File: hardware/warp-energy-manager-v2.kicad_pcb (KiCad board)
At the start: 4 copper layers, 68 x 87 mm, 118 parts, among them J101 Boot, J102 DM3CS, P101 CON-SENSOR2, P102 SG-Ready, P103 L+N, P104 OUT, P105 INPUT, P110 MODBUS, P111 Debug, Q101 2N7002P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

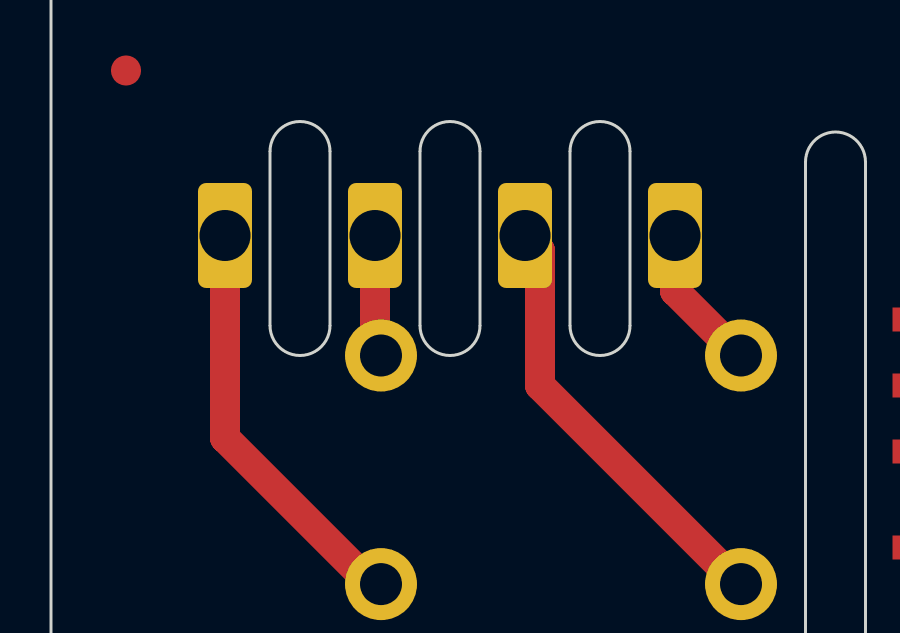
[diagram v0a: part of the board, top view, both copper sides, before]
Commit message: add 3d models
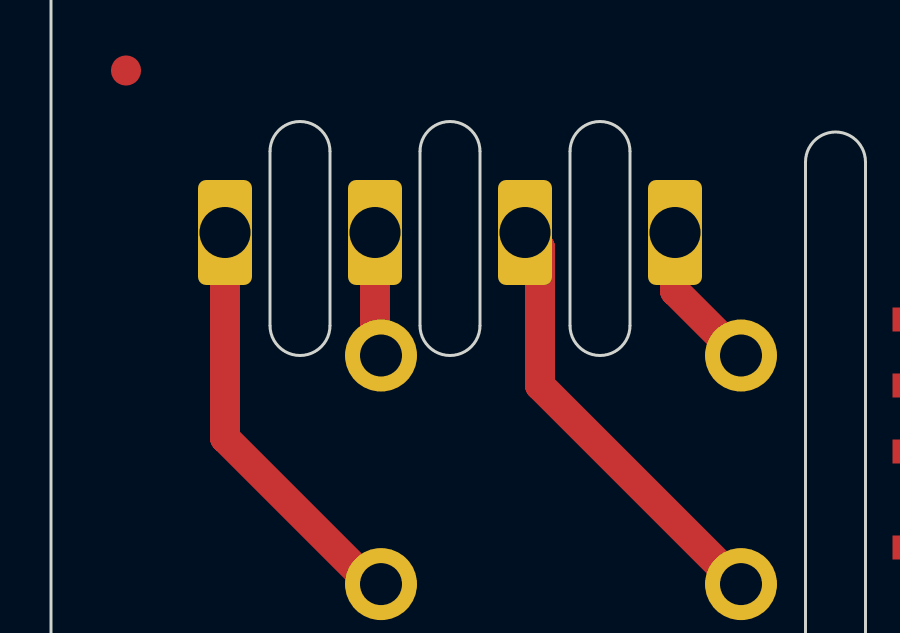
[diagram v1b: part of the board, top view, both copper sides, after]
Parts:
- R104, R105, R115, R116: value 1k -> 2k2
- R112, R117, R120, R121: value 1k -> 680
- moved P104 0.10 mm to (105.7, 61.0)
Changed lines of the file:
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@@
 			(sketchpadsonfab no)
 			(subtractmaskfromsilk yes)
-			(outputformat 3)
+			(outputformat 1)
 			(mirror no)
 			(drillshape 0)
@@
 			(pintype "passive")
 		)
+		(model "${KICAD6_3DMODEL_DIR}/Connectors/OQ_2P_5mm_230V.step"
+			(offset
+				(xyz 0 0 0)
+			)
+			(scale
+				(xyz 1 1 1)
+			)
+			(rotate
+				(xyz 0 0 0)
+			)
+		)
 	)
 	(footprint "kicad-libraries:C0402F"
@@
 		)
 		(property "Value" "100uF"
-			(at 0 1.95072 90)
+			(at -0.00112 0.55 90)
 			(layer "F.Fab")
 			(effects
@@
 		(tags "CMS SOT")
 		(property "Reference" "Q105"
-			(at -0.925 0 180)
+			(at -1.05 0 180)
 			(layer "F.Fab")
 			(effects
@@
 		)
 		(property "Value" "SSM3J355R,LF"
-			(at 0.775 0 180)
+			(at 0.45 0 180)
 			(layer "F.Fab")
 			(effects
@@
 			(pintype "input")
 		)
+		(model "${KICAD6_3DMODEL_DIR}/unsorted/G5Q_1A.step"
+			(offset
+				(xyz 0 0 0)
+			)
+			(scale
+				(xyz 1 1 1)
+			)
+			(rotate
+				(xyz 0 0 0)
+			)
+		)
 	)
 	(footprint "kicad-libraries:MiniMelf"
@@
 			)
 		)
-		(property "Value" "1k"
+		(property "Value" "680"
 			(at 0 -0.4 -90)
 			(layer "F.Fab")
@@
 	(footprint "kicad-libraries:OQ_4P_5mm_230V"
 		(layer "F.Cu")
-		(at 105.65 61.05 180)
+		(at 105.65 60.95 180)
 		(property "Reference" "P104"
 			(at 0 3.5 180)
@@
 			(pintype "passive")
 		)
+		(model "${KICAD6_3DMODEL_DIR}/Connectors/OQ_4P_5mm_230V.step"
+			(offset
+				(xyz 0 0 0)
+			)
+			(scale
+				(xyz 1 1 1)
+			)
+			(rotate
+				(xyz 0 0 0)
+			)
+		)
 	)
 	(footprint "kicad-libraries:SOT23GDS"
@@
 			(pintype "passive")
 		)
+		(model "${KICAD6_3DMODEL_DIR}/unsorted/AGQ2X0.step"
+			(offset
+				(xyz 0 0 0)
+			)
+			(scale
+				(xyz 1 1 1)
+			)
+			(rotate
+				(xyz 0 0 0)
+			)
+		)
 	)
 	(footprint "kicad-libraries:R0603F"
@@
 			)
 		)
-		(property "Value" "1k"
+		(property "Value" "680"
 			(at 0 -0.4 -90)
 			(layer "F.Fab")
@@
 		)
 		(property "Value" "SMAJ12CA"
-			(at -0.71 0.12 0)
+			(at -0.9 0 0)
 			(layer "F.Fab")
 			(effects
@@
 			)
 		)
-		(property "Value" "1k"
+		(property "Value" "680"
 			(at 0 -0.4 -90)
 			(layer "F.Fab")
@@
 			)
 		)
-		(property "Value" "1k"
+		(property "Value" "2k2"
 			(at 0 -0.4 -90)
 			(layer "F.Fab")
@@
 			(pintype "passive")
 		)
+		(model "${KICAD6_3DMODEL_DIR}/unsorted/AGQ2X0.step"
+			(offset
+				(xyz 0 0 0)
+			)
+			(scale
+				(xyz 1 1 1)
+			)
+			(rotate
+				(xyz 0 0 0)
+			)
+		)
 	)
 	(footprint "kicad-libraries:SOT23GDS"
@@
 		(tags "CMS SOT")
 		(property "Reference" "Q101"
-			(at 1 -0.5 0)
+			(at -0.6 0 0)
 			(layer "F.Fab")
 			(effects
@@
 		)
 		(property "Value" "2N7002P"
-			(at 1 0 0)
+			(at 0.8 0 0)
 			(layer "F.Fab")
 			(effects
@@
 			)
 		)
-		(property "Value" "1k"
+		(property "Value" "2k2"
 			(at 0 -0.4 -90)
 			(layer "F.Fab")
@@
 		)
 		(property "Value" "SMAJ12CA"
-			(at -0.71 0.12 180)
+			(at -0.9 0.12 180)
 			(layer "F.Fab")
 			(effects
@@
 			)
 		)
-		(property "Value" "1k"
+		(property "Value" "2k2"
 			(at 0 -0.4 -90)
 			(layer "F.Fab")
@@
 			)
 		)
-		(property "Value" "1k"
+		(property "Value" "680"
 			(at 0 -0.4 -90)
 			(layer "F.Fab")
@@
 			(pintype "input")
 		)
+		(model "${KICAD6_3DMODEL_DIR}/unsorted/G5Q_1A.step"
+			(offset
+				(xyz 0 0 0)
+			)
+			(scale
+				(xyz 1 1 1)
+			)
+			(rotate
+				(xyz 0 0 0)
+			)
+		)
 	)
 	(footprint "kicad-libraries:C0603F"
@@
 		)
 		(property "Value" "SMAJ12CA"
-			(at -0.71 0.12 0)
+			(at -0.9 -0.5 0)
 			(layer "F.Fab")
 			(effects
@@
 			)
 		)
-		(property "Value" "1k"
+		(property "Value" "2k2"
 			(at 0 -0.4 -90)
 			(layer "F.Fab")
@@
 	)
 	(segment
-		(start 115.25 72.65)
-		(end 115.4 72.65)
+		(start 108.15 60.95)
+		(end 108.65 61.45)
 		(width 1)
 		(layer "F.Cu")
@@
 	)
 	(segment
-		(start 108.65 61.55)
-		(end 108.65 66.05)
+		(start 115.25 72.65)
+		(end 115.4 72.65)
 		(width 1)
 		(layer "F.Cu")
@@
 	)
 	(segment
-		(start 108.15 61.05)
-		(end 108.65 61.55)
+		(start 108.65 61.45)
+		(end 108.65 66.05)
 		(width 1)
 		(layer "F.Cu")
@@
 	)
 	(segment
-		(start 113.15 61.05)
+		(start 113.15 60.95)
 		(end 113.15 62.9)
 		(width 1)
@@
 	)
 	(segment
-		(start 98.15 67.8)
-		(end 103.05 72.7)
+		(start 103.05 72.7)
+		(end 103.35 72.7)
 		(width 1)
 		(layer "F.Cu")
@@
 	)
 	(segment
-		(start 103.05 72.7)
-		(end 103.35 72.7)
+		(start 98.15 67.8)
+		(end 103.05 72.7)
 		(width 1)
 		(layer "F.Cu")
@@
 	)
 	(segment
-		(start 98.15 61.05)
+		(start 98.15 60.95)
 		(end 98.15 67.8)
 		(width 1)
@@
 	)
 	(segment
-		(start 103.15 61.05)
+		(start 103.15 60.95)
 		(end 103.15 64.9)
 		(width 1)

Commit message: add descriptions
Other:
- board text added: "230V L N"
- board text added: "Input A IN1 IN2 COM Input B IN1 IN2 COM"
- board text added: "RS485 12V A B GND"
- board text added: "Relais"
- board text added: "Relais COMA NOA COMB NOB"
- board text added: "SG-Ready COM1 NO1 COM2 NO2"
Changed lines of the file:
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@@
-		(layer "Dwgs.User")
-	)
-	(gr_line
-		(start 126.35 45.6)
-		(end 126.35 63.05)
-		(stroke
-			(width 0.1)
-			(type default)
-		)
 		(layer "Dwgs.User")
 	)
@@
 		)
 	)
+	(gr_text "SG-Ready\nCOM1\nNO1\nCOM2\nNO2"
+		(at 131.05 50.15 90)
+		(layer "Dwgs.User")
+		(effects
+			(font
+				(size 1 1)
+				(thickness 0.15)
+			)
+			(justify left bottom)
+		)
+	)
+	(gr_text "Relais\nCOMA\nNOA\nCOMB\nNOB"
+		(at 106.95 49.45 90)
+		(layer "Dwgs.User")
+		(effects
+			(font
+				(size 1 1)
+				(thickness 0.15)
+			)
+			(justify left bottom)
+		)
+	)
+	(gr_text "RS485\n12V\nA\nB\nGND"
+		(at 146.85 144.45 90)
+		(layer "Dwgs.User")
+		(effects
+			(font
+				(size 1 1)
+				(thickness 0.15)
+			)
+			(justify left bottom)
+		)
+	)
+	(gr_text "230V\nL\nN"
+		(at 102.85 143.65 90)
+		(layer "Dwgs.User")
+		(effects
+			(font
+				(size 1 1)
+				(thickness 0.15)
+			)
+			(justify left bottom)
+		)
+	)
+	(gr_text "Input A\nIN1\nIN2\nCOM\n\nInput B\nIN1\nIN2\nCOM"
+		(at 153.65 49.95 90)
+		(layer "Dwgs.User")
+		(effects
+			(font
+				(size 1 1)
+				(thickness 0.15)
+			)
+			(justify left bottom)
+		)
+	)
 	(gr_text "Copyright Tinkerforge GmbH 2024.\nThis documentation describes Open Hardware and is licensed under the\nCERN OHL v. 1.1.\nYou may redistribute and modify this documentation under the terms of the\nCERN OHL v.1.1. (http://ohwr.org/cernohl). This documentation is distributed\nWITHOUT ANY EXPRESS OR IMPLIED WARRANTY, INCLUDING OF\nMERCHANTABILITY, SATISFACTORY QUALITY AND FITNESS FOR A\nPARTICULAR PURPOSE. Please see the CERN OHL v.1.1 for applicable\nconditions"
 		(at 147.85 182.35 0)
@@
 		)
 	)
+	(gr_text "Relais"
+		(at 108.15 43.05 180)
+		(layer "F.Fab")
+		(effects
+			(font
+				(size 1 1)
+				(thickness 0.15)
+			)
+			(justify left bottom)
+		)
+	)

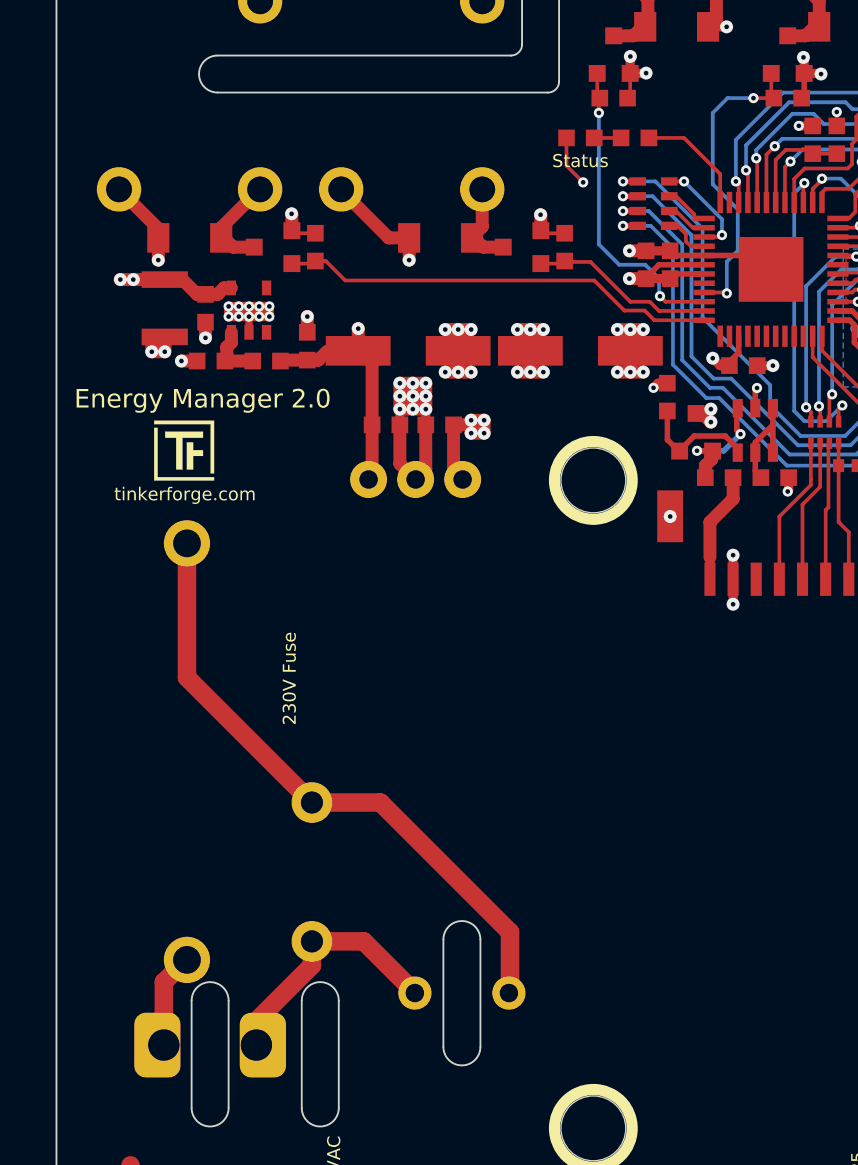
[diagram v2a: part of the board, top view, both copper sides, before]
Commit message: add version 2.1: fix varistor space, fix status led
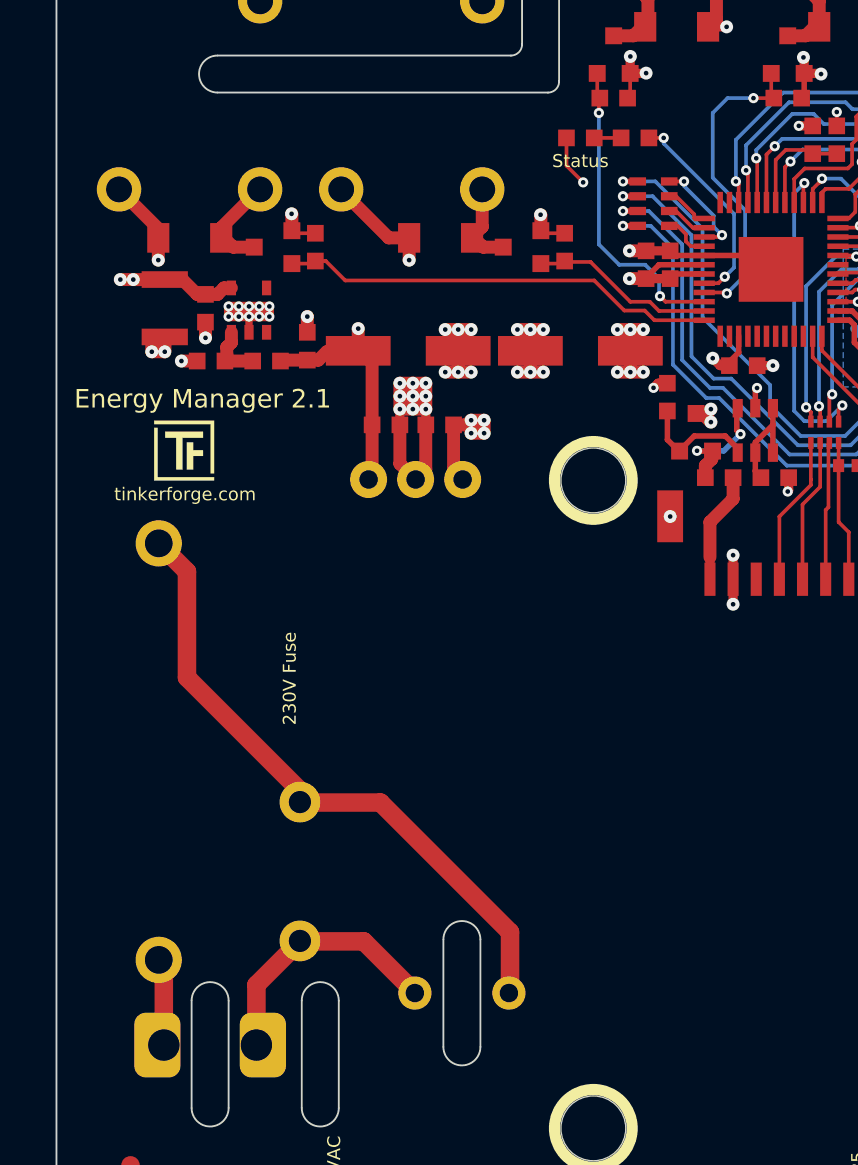
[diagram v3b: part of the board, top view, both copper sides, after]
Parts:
- moved F101 1.53 mm to (97.9, 113.2)
- moved R128 0.65 mm to (105.5, 119.7)
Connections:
- R124 pad 1: Net-(U101D-P2.9_AI) -> Net-(U101C-P1.6_IHO)
- U101 pad 12: Net-(U101D-P2.9_AI) -> unconnected-(U101D-P2.9_AI-Pad12)
- U101 pad 20: unconnected-(U101C-P1.6_IHO-Pad20) -> Net-(U101C-P1.6_IHO)
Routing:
- net Net-(U101C-P1.6_IHO): track 0.00 -> 11.3 mm, vias 0 -> 2
- net Net-(U101D-P2.9_AI): track 6.20 -> 0.00 mm
- net L: track 33.7 -> 34.8 mm
- net Net-(P103-P1): track 5.24 -> 4.72 mm
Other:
- board text added: "Energy Manager 2.1"
- board text removed: "Energy Manager 2.0"
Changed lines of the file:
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@@
 	(title_block
 		(title "Energy Manager Bricklet")
-		(date "2024-06-17")
-		(rev "2.0")
+		(date "2024-07-17")
+		(rev "2.1")
 		(company "Tinkerforge GmbH")
 		(comment 1 "Licensed under CERN OHL v.1.1")
@@
 	(net 60 "unconnected-(U101C-P1.0_IHO-Pad26)")
 	(net 61 "unconnected-(U101B-P0.3_IO-Pad32)")
-	(net 62 "unconnected-(U101C-P1.6_IHO-Pad20)")
+	(net 62 "Net-(U101C-P1.6_IHO)")
 	(net 63 "unconnected-(U101E-P3.0_IO-Pad28)")
 	(net 64 "unconnected-(U101B-P0.0_IO-Pad29)")
@@
 	(net 105 "unconnected-(REL102-Pad4)")
 	(net 106 "unconnected-(REL102-Pad3)")
-	(net 107 "Net-(U101D-P2.9_AI)")
+	(net 107 "unconnected-(U101D-P2.9_AI-Pad12)")
 	(net 108 "unconnected-(U101B-P0.2_IO-Pad31)")
 	(net 109 "Net-(C112-Pad1)")
@@
 	(footprint "kicad-libraries:VAR_10mm"
 		(layer "F.Cu")
-		(at 106.15 119.7 -90)
+		(at 105.5 119.675 -90)
 		(property "Reference" "R128"
 			(at 0 0.95 90)
@@
 			(size 0.9 0.9)
 			(layers "F.Cu" "F.Paste" "F.Mask")
-			(net 107 "Net-(U101D-P2.9_AI)")
+			(net 62 "Net-(U101C-P1.6_IHO)")
 			(pintype "passive")
 		)
@@
 			(size 0.29972 1.14808)
 			(layers "F.Cu" "F.Paste" "F.Mask")
-			(net 107 "Net-(U101D-P2.9_AI)")
+			(net 107 "unconnected-(U101D-P2.9_AI-Pad12)")
 			(pinfunction "P2.9_AI")
-			(pintype "passive")
+			(pintype "passive+no_connect")
 		)
 		(pad "13" smd rect
@@
 			(size 0.29972 1.14808)
 			(layers "F.Cu" "F.Paste" "F.Mask")
-			(net 62 "unconnected-(U101C-P1.6_IHO-Pad20)")
+			(net 62 "Net-(U101C-P1.6_IHO)")
 			(pinfunction "P1.6_IHO")
-			(pintype "passive+no_connect")
+			(pintype "passive")
 		)
 		(pad "21" smd rect
@@
 	(footprint "kicad-libraries:Fuse-Holder-5x20"
 		(layer "F.Cu")
-		(at 99.4 113.2 90)
+		(at 97.875 113.2 90)
 		(property "Reference" "F101"
 			(at 0 0.5 -90)
@@
 		)
 		(property "Value" "SMAJ12CA"
-			(at -0.9 0 0)
+			(at -0.71 0.12 0)
 			(layer "F.Fab")
 			(effects
@@
 		)
 		(property "Value" "SMAJ12CA"
-			(at -0.9 0.12 180)
+			(at -0.71 0.12 180)
 			(layer "F.Fab")
 			(effects
@@
 		)
 		(property "Value" "SMAJ12CA"
-			(at -0.9 -0.5 0)
+			(at -0.71 0.12 0)
 			(layer "F.Fab")
 			(effects
@@
 		)
 	)
-	(gr_text "Energy Manager 2.0"
+	(gr_text "Energy Manager 2.1"
 		(at 100.25 94.15 0)
 		(layer "F.SilkS")
@@
 	)
 	(segment
-		(start 99.4 109.2)
-		(end 106.15 115.95)
+		(start 105.5 115.95)
+		(end 109.85 115.95)
 		(width 1)
 		(layer "F.Cu")
@@
 	(segment
 		(start 116.85 122.95)
-		(end 109.85 115.95)
+		(end 116.85 126.25)
+		(width 1)
+		(layer "F.Cu")
+		(net 8)
+	)
+	(segment
+		(start 105.475 115.275)
+		(end 105.475 115.975)
+		(width 1)
+		(layer "F.Cu")
+		(net 8)
+	)
+	(segment
+		(start 99.4 109.2)
+		(end 105.475 115.275)
 		(width 1)
 		(layer "F.Cu")
@@
 	)
 	(segment
-		(start 99.4 101.95)
+		(start 99.4 103.475)
 		(end 99.4 109.2)
 		(width 1)
@@
 	(segment
 		(start 109.85 115.95)
-		(end 106.15 115.95)
+		(end 116.85 122.95)
 		(width 1)
 		(layer "F.Cu")
@@
 	)
 	(segment
-		(start 116.85 126.25)
-		(end 116.85 122.95)
+		(start 97.875 101.95)
+		(end 99.4 103.475)
+		(width 1)
+		(layer "F.Cu")
+		(net 8)
+	)
+	(segment
+		(start 105.475 115.975)
+		(end 105.5 115.95)
 		(width 1)
 		(layer "F.Cu")
@@
 	)
 	(segment
-		(start 111.75 126.25)
-		(end 108.95 123.45)
+		(start 103.15036 125.79964)
+		(end 105.5 123.45)
 		(width 1)
 		(layer "F.Cu")
@@
 	)
 	(segment
-		(start 103.15036 127.74964)
-		(end 106.15 124.75)
+		(start 105.5 123.45)
+		(end 108.95 123.45)
 		(width 1)
 		(layer "F.Cu")
@@
 	)
 	(segment
-		(start 106.15 124.75)
-		(end 106.15 123.45)
+		(start 103.15036 129.05106)
+		(end 103.15036 125.79964)
 		(width 1)
 		(layer "F.Cu")
@@
 	(segment
 		(start 108.95 123.45)
-		(end 106.15 123.45)
-		(width 1)
-		(layer "F.Cu")
-		(net 12)
-	)
-	(segment
-		(start 103.15036 129.05106)
-		(end 103.15036 127.74964)
+		(end 111.75 126.25)
 		(width 1)
 		(layer "F.Cu")
@@
 	)
 	(segment
-		(start 98.15036 125.64964)
-		(end 99.45 124.35)
+		(start 98.15036 124.72536)
+		(end 97.875 124.45)
 		(width 1)
 		(layer "F.Cu")
@@
 	(segment
 		(start 98.15036 129.05106)
-		(end 98.15036 125.64964)
+		(end 98.15036 124.72536)
 		(width 1)
 		(layer "F.Cu")
@@
 	)
 	(segment
-		(start 128.3 84.45)
+		(start 126.25 82.65)
 		(end 126.25 82.4)
 		(width 0.2)
@@
 	)
 	(segment
+		(start 127.85 84.85)
+		(end 127.85 84.25)
+		(width 0.2)
+		(layer "B.Cu")
+		(net 32)
+	)
+	(segment
+		(start 127.85 84.25)
+		(end 126.25 82.65)
+		(width 0.2)
+		(layer "B.Cu")
+		(net 32)
+	)
+	(segment
 		(start 128.3 85.3)
-		(end 128.3 84.45)
+		(end 127.85 84.85)
 		(width 0.2)
 		(layer "B.Cu")
@@
 	)
 	(segment
+		(start 125.15 80.05)
+		(end 124.35 80.05)
+		(width 0.2)
+		(layer "F.Cu")
+		(net 62)
+	)
+	(segment
+		(start 128.1007 87.8993)
+		(end 128.45 87.55)
+		(width 0.2)
+		(layer "F.Cu")
+		(net 62)
+	)
+	(segment
+		(start 127.33812 87.8993)
+		(end 128.1007 87.8993)
+		(width 0.2)
+		(layer "F.Cu")
+		(net 62)
+	)
+	(via
+		(at 125.15 80.05)
+		(size 0.55)
+		(drill 0.25)
+		(layers "F.Cu" "B.Cu")
+		(net 62)
+	)
+	(via
+		(at 128.45 87.55)
+		(size 0.55)
+		(drill 0.25)
+		(layers "F.Cu" "B.Cu")
+		(net 62)
+	)
+	(segment
+		(start 125.15 80.35)
+		(end 125.15 80.05)
+		(width 0.2)
+		(layer "B.Cu")
+		(net 62)
+	)
+	(segment
+		(start 128.45 87.55)
+		(end 128.95 87.05)
+		(width 0.2)
+		(layer "B.Cu")
+		(net 62)
+	)
+	(segment
+		(start 128.95 87.05)
+		(end 128.95 84.15)
+		(width 0.2)
+		(layer "B.Cu")
+		(net 62)
+	)
+	(segment
+		(start 128.95 84.15)
+		(end 125.15 80.35)
+		(width 0.2)
+		(layer "B.Cu")
+		(net 62)
+	)
+	(segment
 		(start 150.75 90.45)
 		(end 145.05 84.75)
@@
 	)
 	(segment
-		(start 129.15 83.9)
-		(end 127.8 82.55)
-		(width 0.2)
-		(layer "B.Cu")
-		(net 83)
-	)
-	(segment
-		(start 127.8 82.55)
-		(end 127.8 78.7)
+		(start 128.6 77.9)
+		(end 130 77.9)
 		(width 0.2)
 		(layer "B.Cu")
@@
 	)
 	(segment
-		(start 128.561218 86.738782)
-		(end 129.15 86.15)
+		(start 129.55 83.95)
+		(end 127.8 82.2)
 		(width 0.2)
 		(layer "B.Cu")
@@
 	)
 	(segment
-		(start 127.8 78.7)
-		(end 128.6 77.9)
+		(start 127.8 82.2)
+		(end 127.8 78.7)
 		(width 0.2)
 		(layer "B.Cu")
@@
 	(segment
 		(start 128.561218 88.448922)
-		(end 128.561218 86.738782)
+		(end 129.55 87.46014)
 		(width 0.2)
 		(layer "B.Cu")
@@
 	)
 	(segment
-		(start 129.15 86.15)
-		(end 129.15 83.9)
+		(start 127.8 78.7)
+		(end 128.6 77.9)
 		(width 0.2)
 		(layer "B.Cu")
@@
 	)
 	(segment
-		(start 128.6 77.9)
-		(end 130 77.9)
+		(start 129.55 87.46014)
+		(end 129.55 83.95)
 		(width 0.2)
 		(layer "B.Cu")
@@
 	)
 	(segment
-		(start 128.20172 82.00172)
-		(end 126.25 80.05)
-		(width 0.2)
-		(layer "F.Cu")
-		(net 107)
-	)
-	(segment
-		(start 126.25 80.05)
-		(end 124.35 80.05)
-		(width 0.2)
-		(layer "F.Cu")
-		(net 107)
-	)
-	(segment
-		(start 128.20172 83.53812)
-		(end 128.20172 82.00172)
-		(width 0.2)
-		(layer "F.Cu")
-		(net 107)
-	)
-	(segment
